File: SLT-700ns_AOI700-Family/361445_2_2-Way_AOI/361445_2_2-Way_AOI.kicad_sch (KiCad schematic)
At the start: 17 parts, among them T1 CB, U1 16-Pin_SLx_Can

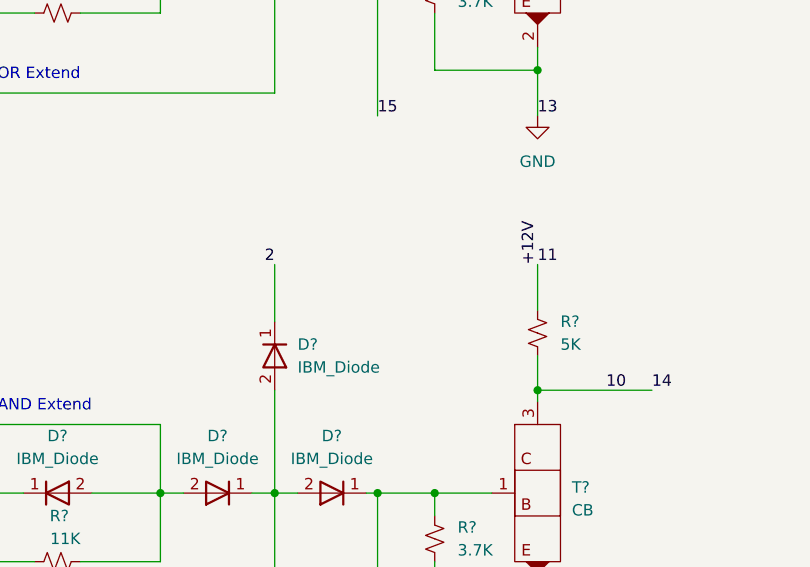
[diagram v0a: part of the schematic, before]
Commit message: Add can P/N to schematics for SLT-700
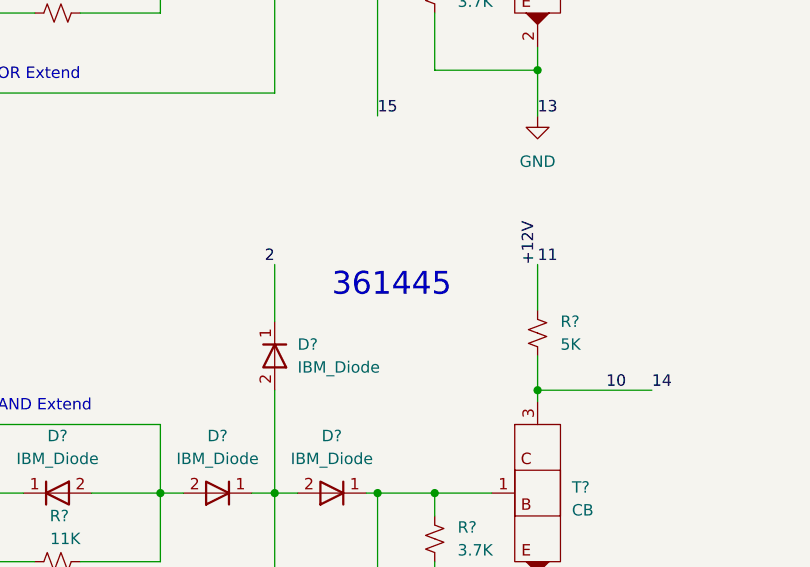
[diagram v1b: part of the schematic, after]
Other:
- note added: "361445"
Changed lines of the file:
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@@
     (effects (font (size 1.27 1.27)) (justify right bottom))
+  )
+  (text "361445" (at 95.25 111.76 0)
+    (effects (font (size 2.54 2.54)) (justify left bottom))
   )
   (text "OR Extend" (at 67.31 87.63 180)
